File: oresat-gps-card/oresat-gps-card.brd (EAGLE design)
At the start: 99.8 x 94.7 mm, 354 parts, among them J1 ORESAT-DEBUG-CONNECTOR-CARD, J100 DM3BT-DSF-PEJS, J102 FTSH-105-XX-X-DV-K, J4 TFM-120-01-L-D-RA, Q1 MMBT2907, Q2 PMV45EN, Q3 DMP2240UDM, Q4 PMV45EN, Q5 MOSFET-PCH-SOT23-6, Q6 MOSFET-PCH-SOT23-6, U1 RCLAMP0504FB, U10 TLVH431, U11 TCAN330, U12 MIC842LYC5, U13 MIC842LYC5, U14 MAX4211FETE, U15 TPS62112, U16 MAX7310ATE, U17 25AAXX, U18 VENUS838FLPX-L, U19 BP2G+, U2 TPS2051CDBVR, U20 MAX8510EXK29+T, U21 ALM-GP003, U22 LT1719S6, U4 SN74LVC1G07DCK, U5 MAX2769ETI+, U6 7Q-16.368MBG-T, U7 OSD3358-512M-BSM, U8 MAX8510EXK29+T, U9 MAX8510EXK29+T, Y1 24MHz, Y2 ABS07-32.768KHZ-T

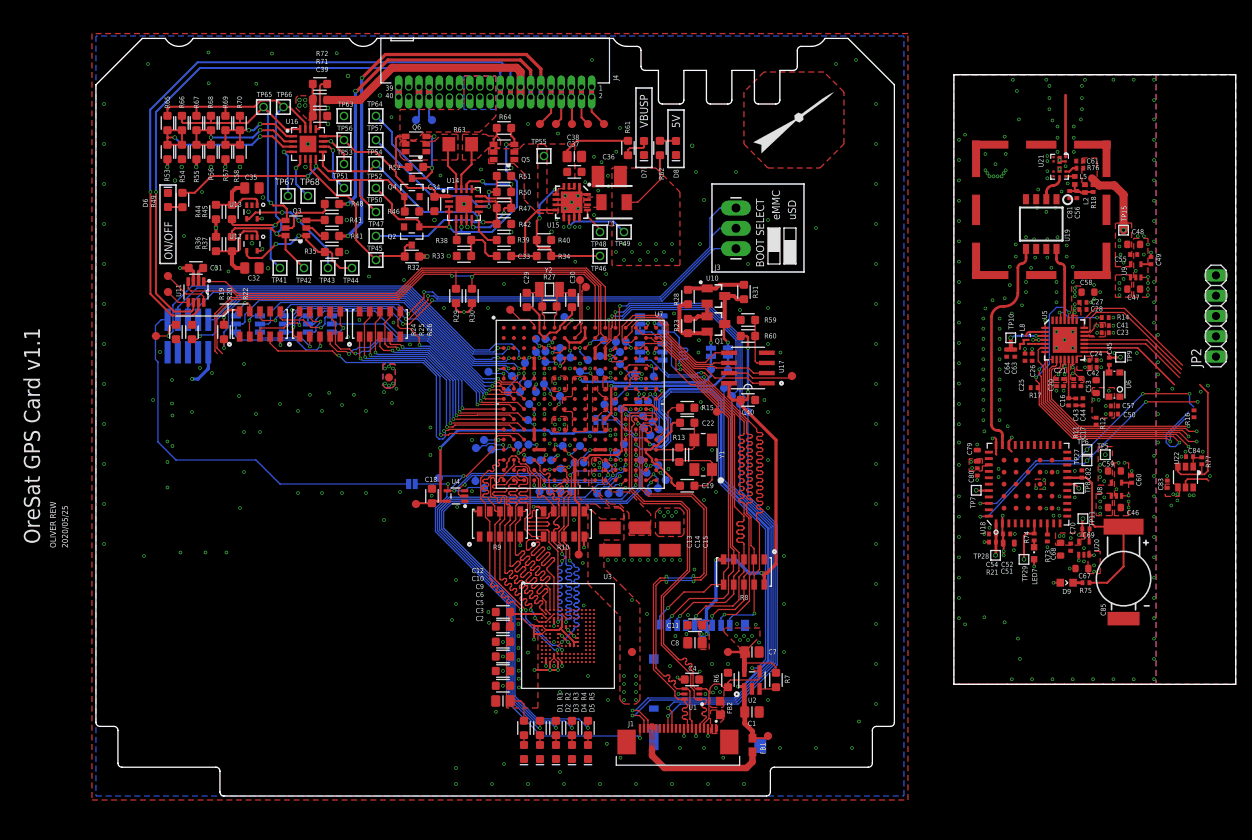
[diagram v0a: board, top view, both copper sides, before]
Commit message: GPS card has been mostly layed out. Still missing a few things, but nothing major.
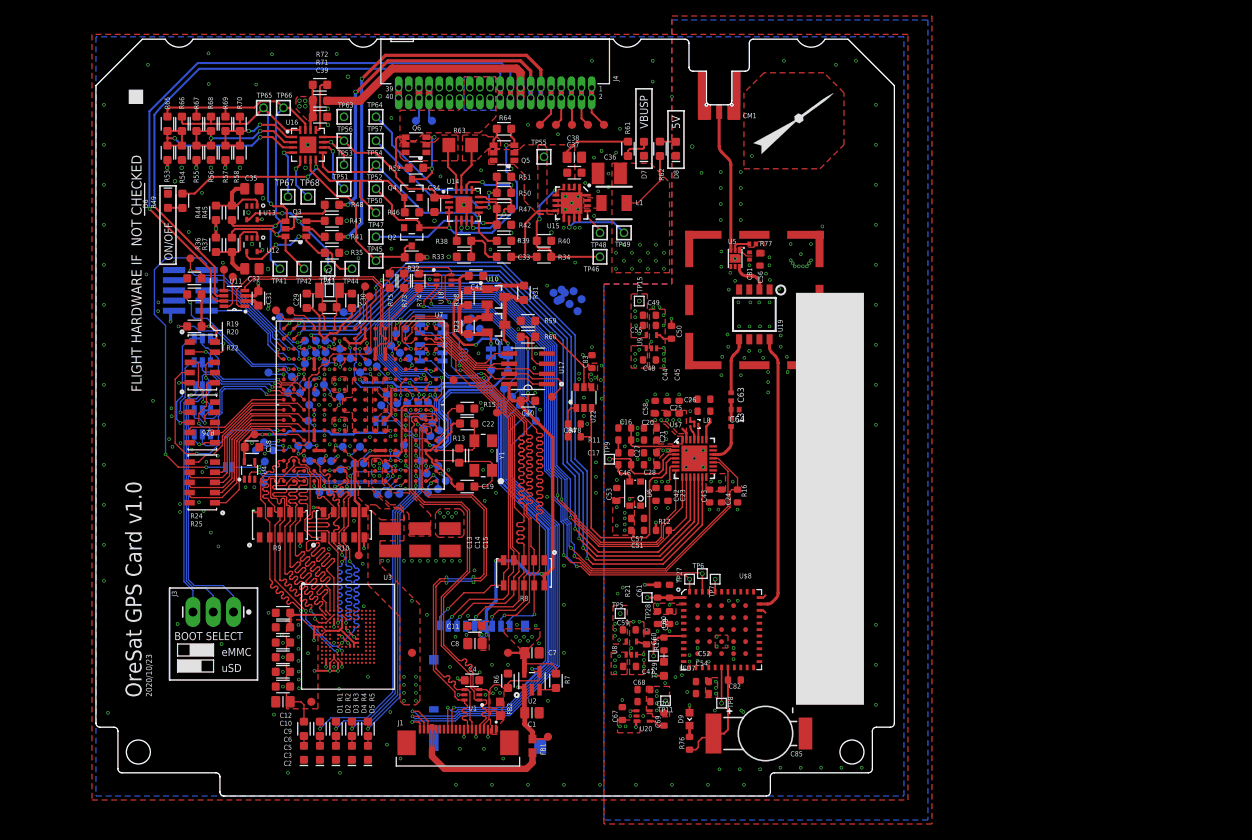
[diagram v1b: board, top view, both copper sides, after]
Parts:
- removed JP2: (no value), pinhead:1X05
- removed L2: 22n, rcl_custom:.0402-B-NOSILK
- removed L5: 1.8n, rcl_custom:.0402-B-NOSILK
- removed R14: 1k, rcl_custom:0402-C-NOSILK@1
- removed R18: 10, rcl_custom:0402-C-NOSILK@1
- removed R29, R30: 4.7k, oresat-rcl:.0603-A
- removed U21: ALM-GP003, ic-lna-ALM-GPxx-Avago:AVAGO+SAW+LNA
- added CM1: J-MOLEX-SMPM-73300-003X, J-Molex-73300-003X-SMPM-M-edge-mount:J-MOLEX-SMPM-073300-003X
- added L3: 5.6n, oresat-rcl:.0402-B-NOSILK
- added R78: 10k, oresat-rcl:.0603-B-NOSILK
- added TP12, TP13, TP16, TP17, TP18, TP19, TP20, TP21, TP23, TP24, TP26, TP32, TP33, TP34, TP36, TP37, TP70: TEST-POINT3X4, SparkFun-Connectors:PAD.03X.04
- added U$4: (no value), oresat-flight-marker:FLIGHTMARKER_OLD_BOARDS
- added U$7: MAX2771ETI+, U-Maxim-MAX2771-Multiband-Universal-GNSS-Receiver:90-0023
- added U$8: VENUS838LPX-L, U-Venus-Venus838LPxL-GPS-Module:VENUS838LPX
- C16, C17, C20, C21, C23, C24, C25, C26, C27, C28, C42, C43, C55, C56, C57, C60, C69, C70, C80, C82, C83, C84: device rcl_custom:.0402-C-NOSILK -> oresat-rcl:.0603-B-NOSILK
- C41: value 100p -> 0.1uF; device rcl_custom:.0402-C-NOSILK -> oresat-rcl:.0603-A
- C44, C54: value 100n -> 100p; device rcl_custom:.0402-C-NOSILK -> oresat-rcl:.0603-B-NOSILK
- C45: value 10n -> 100n; device rcl_custom:.0402-C-NOSILK -> oresat-rcl:.0603-B-NOSILK
- C46: value 1u -> 10n; device rcl_custom:.0603-B-NOSILK -> oresat-rcl:.0603-B-NOSILK
- C49: value 10n -> 1u; device rcl_custom:.0402-C-NOSILK -> rcl_custom:.0603-B-NOSILK
- C50: value 100n -> 10n; device rcl_custom:.0402-C-NOSILK -> oresat-rcl:.0603-B-NOSILK
- C51: value 1u -> 100n; device rcl_custom:.0603-C-NOSILK -> oresat-rcl:.0603-B-NOSILK
- C52: value 100p -> 1u; device rcl_custom:.0402-C-NOSILK -> oresat-rcl:.0603-B-NOSILK
- C53: device rcl_custom:.0603-B-NOSILK -> oresat-rcl:.0603-B-NOSILK
- C61: value 330p -> 100n; device rcl_custom:.0402-C-NOSILK -> oresat-rcl:.0603-B-NOSILK
- C63: value 100p -> 470p; device rcl_custom:.0402-C-NOSILK -> oresat-rcl:.0402-B-NOSILK
- C64: value 100n -> 1.7p; device rcl_custom:.0402-C-NOSILK -> oresat-rcl:.0402-B-NOSILK
- C79: device rcl_custom:.0603-C-NOSILK -> oresat-rcl:.0603-B-NOSILK
- C81: value 47p -> 56p
- JP107: value JUMPER-SMT_3_NO_NO_SILK -> JUMPER-SMT_3_NO_SILK; device SparkFun-Jumpers:SMT-JUMPER_3_0-NO_TRACE_NO-SILK -> SparkFun-Jumpers:SMT-JUMPER_3_NO_SILK
- LED7: value YLW -> Yellow; device led:CHIPLED_0603 -> SparkFun-LED:LED-0603
- PCB1: value ORESAT-CARD-V1.2-GENERIC-3XRF-V1.0 -> ORESAT-CARD-V1.3-GENERIC-1RF-POS2; device oresat-cards:ORESAT-CARD-V1.2-GENERIC-3XRF-V1.0 -> oresat-cards:ORESAT-CARD-V1.3-GENERIC-1RF-POS2
- R11, R12, R16, R21: device rcl_custom:0402-C-NOSILK@1 -> oresat-rcl:.0603-B-NOSILK
- R17: value 10k -> 1k; device rcl_custom:0402-C-NOSILK@1 -> oresat-rcl:.0603-B-NOSILK
- R73: value 10k -> 100; device rcl_custom:0402-C-NOSILK@1 -> oresat-rcl:.0603-A
- R74: value 1k -> 100; device rcl_custom:0402-C-NOSILK@1 -> oresat-rcl:.0603-A
- R75: device rcl_custom:0402-C-NOSILK@1 -> oresat-rcl:.0603-A
- R76: value 4.7k -> 100; device rcl_custom:0402-C-NOSILK@1 -> oresat-rcl:.0603-B-NOSILK
- TP10: value TEST-POINT15MIL-TEST-POINT -> TEST-POINT3X4; device Tova:15MIL-TEST-POINT -> SparkFun-Connectors:PAD.03X.04
- U18: value VENUS838FLPX-L -> RCLAMP0504FB; device SparkFun-RF:VENUS638FLPX -> U-Semtec-RCLAMP0504FB:SC70-6
- U5: value MAX2769ETI+ -> SKY65723-81; device max2769:90-0023 -> U-Skyworks-SKY65723-81-GPS-LNA-with-filter:SKY65723-81
- moved R75 94.9 mm to (36.7, 64.4), turned to 270 degrees
- moved R76 86.9 mm to (74.2, 6.59), turned to 90 degrees
- moved R73 86.6 mm to (38.5, 64.4), turned to 270 degrees
- moved R74 83.3 mm to (40.3, 64.4), turned to 270 degrees
- moved J3 80.6 mm to (17.2, 23.0), turned to 180 degrees
- moved C41 78.9 mm to (47.5, 65.0)
- moved C47 78.7 mm to (66.7, 16.2)
- moved U18 77.3 mm to (43.5, 64.5), turned to 270 degrees
- moved C84 77.0 mm to (59.8, 46.5), turned to 0 degrees
- moved U22 75.8 mm to (61.0, 49.8), turned to 180 degrees
- moved C61 74.3 mm to (71.7, 25.6), turned to 270 degrees
- moved C83 73.5 mm to (62.0, 54.3)
- moved TP9 65.1 mm to (64.2, 42.1)
- moved C59 63.8 mm to (66.7, 20.8)
- moved C60 63.8 mm to (68.8, 19.8)
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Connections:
- net SPARE5 renamed N$103
- removed net 3.3VD: C46.1, C47.1, C67.1, C83.1, U20.1, U20.3, U22.4, U8.1, U8.3, U9.1, U9.3
- removed net ANTBIAS: C63.1, C64.1, TP10.P$1, U5.3
- removed net D0_I: JP102.1
- removed net D1_I: JP103.1
- removed net D2_I: JP110.1
- removed net D3_I: JP111.1
- removed net LED/GPIO: R74.2, TP29.P$1, U18.7
- removed net LNA-POWER-FILTERED: C56.1, C81.1, L2.1, L5.1, R18.2
- removed net MAX_!IDLE: R17.2, U5.24
- removed net MAX_ANTFLAG: U5.1
- removed net MAX_CFG_!CS: R12.1, U5.10
- removed net MAX_CFG_SPI2_MOSI: U5.8
- removed net MAX_CFG_SPI2_SCLK: U5.9
- removed net N$103 (its old number): L5.2, U21.7
- removed net N$117 (its old number): C45.1, U6.3
- removed net N$118 (its old number): C84.1, R77.1, U22.1
- removed net N$119 (its old number): R73.2, U18.9
- removed net N$21 (its old number): U21.1
- removed net N$32 (its old number): C18.1, JP104.1, TP14.P$1, TP164.P$1, U4.5, U7.K11, U7.L11
- removed net N$50 (its old number): TP143.P$1, U7.J14
- removed net N$97: TP148.P$1, U7.G14
- removed net PGM: R14.1, U5.26
- removed net RTC: TP8.P$1, U18.17
- removed net SCL_2: R30.2, U7.A10
- removed net SDA_2: R29.2, U7.B10
- removed net STM_USART6_RX: TP27.P$1, U18.44
- removed net STM_USART6_TX: TP6.P$1, U18.42
- new net 3.3VA: C18.1, C41.1, JP104.1, TP14.P$1, TP164.P$1, U18.5, U4.5, U7.K11, U7.L11
- new net LED: R17.2, TP29.P$1, U$8.7
- new net N$114: R74.2, U7.C11, U7.D11
- new net N$115: R75.2, U7.M2
- new net N$116: R73.2, U7.C10, U7.D10
- new net N$123: C63.2, C64.2, L3.1
- new net N$124: L3.2, U$7.19
- new net N$125: LED7.C, R17.1
- new net N$126: D9.CATHODE, R76.2
- new net N$127: TP8.P$1, U$8.17
- new net N$129: TP13.P$1, U7.D16
- new net N$130: TP16.P$1, U7.D15
- new net N$131: TP17.P$1, U7.D14
- new net N$133: TP19.P$1, U7.F16
- new net N$15: TP23.P$1, U7.C4
- new net N$16: TP24.P$1, U7.C3
- new net N$17: TP26.P$1, U7.B3
- new net N$18: TP32.P$1, U7.A3
- new net RF-IN: CM1.RF, U5.3
- new net SPI1_CS0: R12.1, TP143.P$1, U$7.9, U7.J14
- new net SPI1_D0: TP36.P$1, U$7.7, U7.F14
- new net SPI1_D1: TP18.P$1, U7.E15
- new net SPI1_SCLK: TP37.P$1, U$7.8, U7.F15
- new net UART2_RX: TP147.P$1, TP27.P$1, U$8.44, U7.H16
- new net UART2_TX: TP10.P$1, TP6.P$1, U$8.42, U7.E16
- net 2.85V-S: now also C54.1, U$8.2, U$8.58; no longer C51.1, U18.2, U18.36, U18.58
- net 2.85VA: now also C45.1, C50.1, C56.1, C81.1, R77.1, U$7.2, U$7.22, U$7.27, U$7.28, U5.1; no longer C43.1, C48.1, C61.1, L2.2, R18.1, R76.1, U5.11, U5.13, U5.23, U5.4
- net 2.85VD: now also C43.1, C51.1, U$7.14, U$7.6; no longer C41.1, C50.1, U5.14, U5.19
- net 3.3V: now also C47.1, C48.1, C67.1, C83.1, U20.1, U20.3, U22.4, U8.1, U8.3, U9.1, U9.3; no longer R29.1, R30.1
- net AGND: now also C45.2, C51.2, C64.1, CM1.P$1, CM1.P$2, CM1.P$3, CM1.P$4, U$7.BODY, U$8.21, U$8.22, U$8.24, U$8.25, U$8.27, U$8.28, U$8.29, U$8.31, U$8.33, U$8.61, U$8.62, U$8.65, U$8.69, U5.GND; no longer C43.2, C50.2, C61.2, C63.2, C64.2, U18.21, U18.22, U18.24, U18.25, U18.27, U18.28, U18.29, U18.31, U18.33, U18.61, U18.62, U18.65, U18.69, U21.2, U21.3, U21.4, U21.9, U21.P$1, U21.P$2, U5.BODY
- net CPOUT: now also U$7.1; no longer U5.12
- net EEPROM_WP: now also R75.1, U18.6; no longer U7.M2
- net GND: now also C43.2, C49.2, C54.2, C61.1, U$8.10, U$8.11, U$8.15, U$8.19, U$8.4, U$8.49, U$8.5, U$8.6, U$8.60, U$8.64, U18.2; no longer C46.2, C51.2, C54.1, R14.2, R17.1, R73.1, U18.10, U18.11, U18.15, U18.19, U18.49, U18.60, U18.64
- net I0: now also TP21.P$1, U$7.12, U7.A2; no longer JP2.4, U5.20
- net I1: now also TP20.P$1, U$7.13, U7.A1; no longer JP2.5, U5.21
- net I2C0_SCL: now also R73.1, U18.3; no longer U7.C10, U7.D10
- net I2C0_SDA: now also R74.1, U18.1; no longer U7.C11, U7.D11
- net LNAOUT: now also U$7.24; no longer U5.2
- net MAX-CLKOUT: now also U7.B4; no longer JP2.1
- net MAX-RF: now also C63.1, U19.5; no longer U19.8, U5.25
- net MAX_!SHDN: now also TP148.P$1, U$7.18, U7.G14; no longer U5.7
- net MAX_CLK_OUT: now also R78.2, U$7.4; no longer R77.2, U5.16
- net MAX_LD: now also TP70.P$1, U$7.17, U7.G15; no longer U5.6
- net MIXIN: now also U$7.25; no longer U5.5
- net N$113: now also C50.2; no longer C49.2
- net N$120: now also C46.1, U6.3; no longer LED7.C, R74.1
- net N$121: now also C84.1, R78.1, U22.1; no longer D9.CATHODE, R75.2
- net N$19: now also U5.6; no longer U21.6
- net N$24: now also R77.2, U5.2; no longer R76.2, U21.8
- net N$53: now also TP12.P$1, U7.E14; no longer TP147.P$1, U7.H16
- net Q0: now also TP34.P$1, U$7.11, U7.B1; no longer JP2.3, U5.18
- net Q1: now also TP33.P$1, U$7.10, U7.B2; no longer JP2.2, U5.17
- net STQ-!RST: now also C61.2, U$8.1; no longer C54.2, U18.1
- net STQ-PPS: now also U$8.40; no longer U18.40
- net STQ-RF: now also U$8.32, U19.8; no longer U18.32, U19.5
- net STQ-VBAT: now also R76.1, U$8.18; no longer R75.1, U18.18
- net XTAL: now also C46.2, U$7.3; no longer C45.2, U5.15
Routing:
- net SPI1_CS0: track 0.00 -> 92.5 mm, vias 0 -> 2
- net UART2_RX: track 0.00 -> 84.6 mm, vias 0 -> 2
- net UART2_TX: track 0.00 -> 81.6 mm, vias 0 -> 2
- net SPI1_D0: track 0.00 -> 80.5 mm, vias 0 -> 2
- net SPI1_SCLK: track 0.00 -> 79.7 mm, vias 0 -> 2
- net I1: track 16.8 -> 94.8 mm, vias 0 -> 2
- net Q0: track 13.8 -> 90.7 mm, vias 0 -> 2
- net I0: track 17.0 -> 91.2 mm, vias 0 -> 2
- net Q1: track 13.6 -> 87.1 mm, vias 0 -> 2
- net MAX_!SHDN: track 27.2 -> 99.2 mm, vias 1 -> 3
- net MAX_LD: track 28.3 -> 96.2 mm, vias 1 -> 2
- net SDA_2: track 64.7 -> 0.00 mm
- net 3.3VA: track 0.00 -> 64.5 mm, vias 0 -> 5
- net SCL_2: track 62.3 -> 0.00 mm, vias 2 -> 0
- net N$32 (its old number): track 56.0 -> 0.00 mm, vias 3 -> 0
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- added copper zone on layer 1, net 2.85VS
- added copper zone on layer 1, net 3.3VA
- removed copper zone on layer 1, net N$32 (its old number)
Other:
- board size 99.8 x 94.7 mm -> 99.8 x 94.6 mm
- board text added: "10.5mm Solar Card Opening"
- board text added: "2020/10/23"
- board text added: "Min. Cable Length: 28.625mm FFC Cable: Molex 0151660381 29.97mm"
- board text added: "OreSat GPS Card v1.0"
- board text removed: "2020/05/25"
- board text removed: "CAMERA"
- board text removed: "OLIVER REW"
- board text removed: "OreSat GPS Card v1.1"

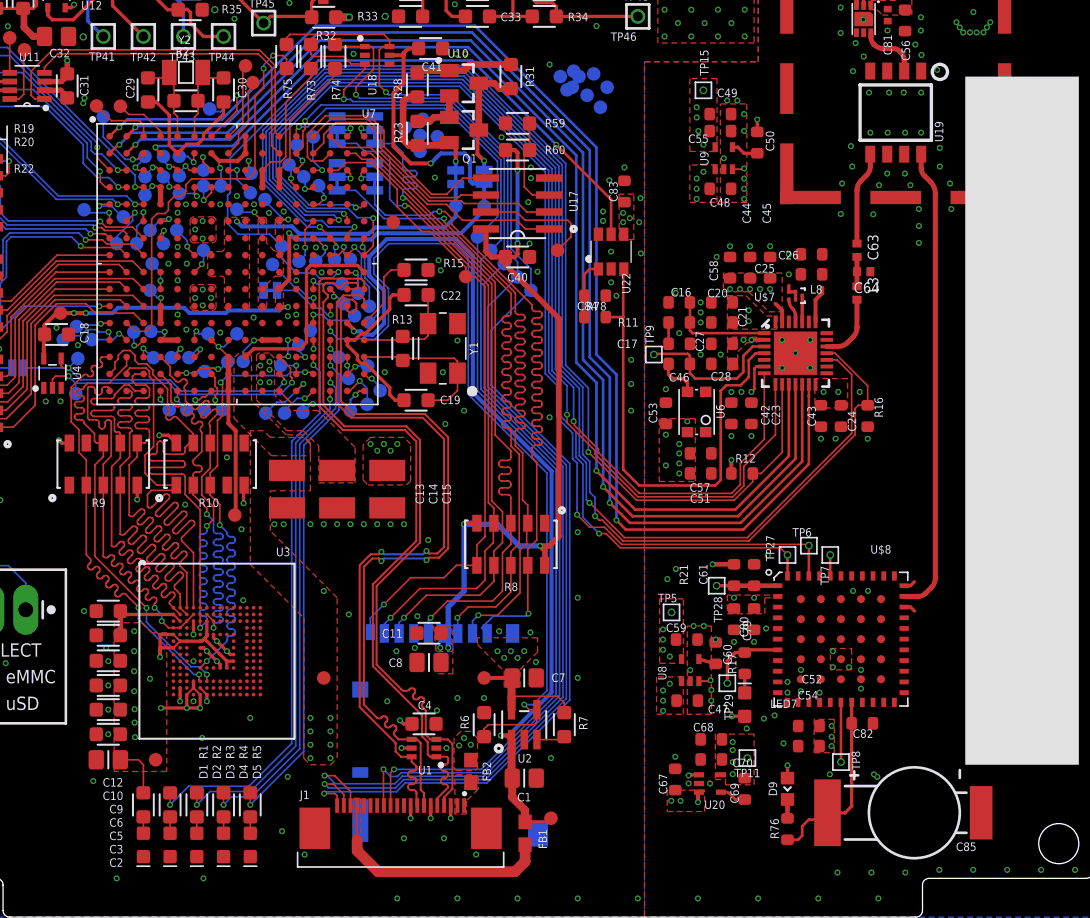
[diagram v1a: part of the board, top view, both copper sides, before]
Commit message: Added some polygons to the power plane
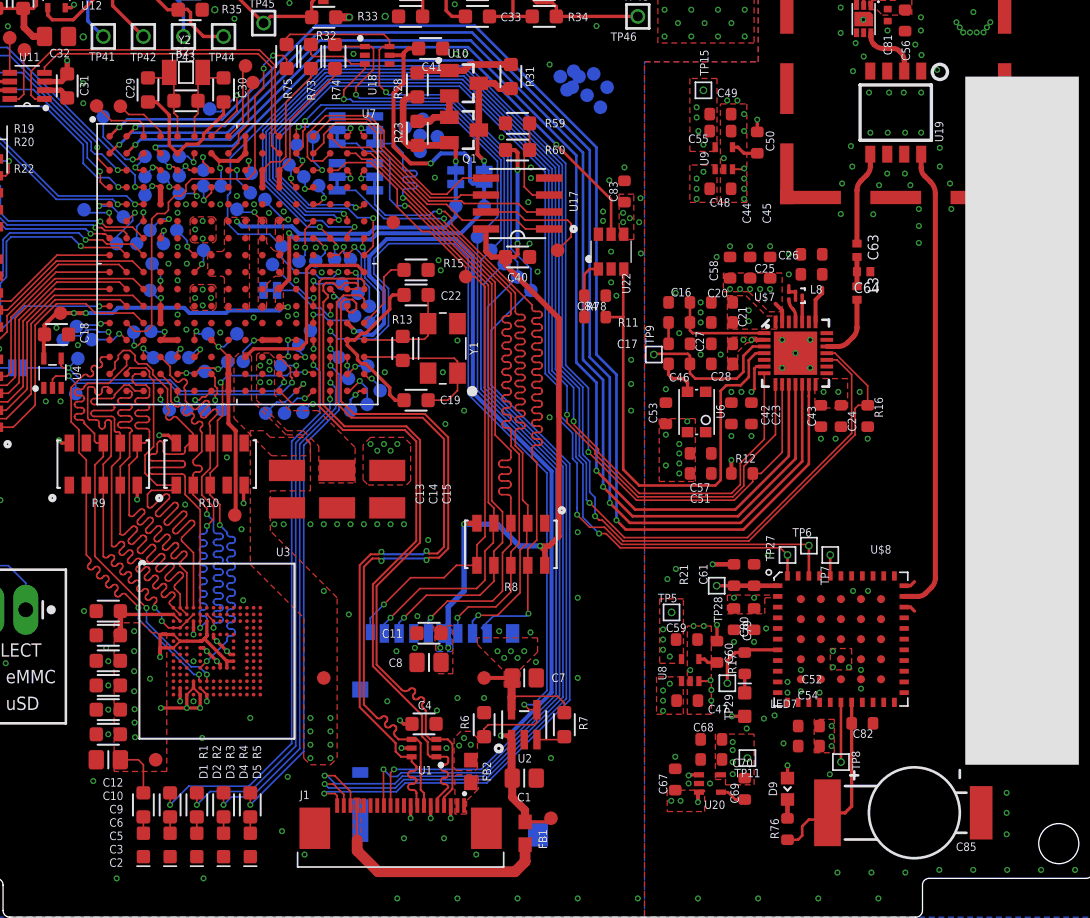
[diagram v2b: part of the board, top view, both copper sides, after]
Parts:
- moved C60 0.14 mm to (68.9, 19.9)
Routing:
- net 2.85VD: track 4.11 -> 5.11 mm
- net GND: vias 368 -> 369
- net 3.3V: vias 34 -> 45
- removed copper zone on layer 1, net 3.3VD
- removed copper zone on layer 15, net 3.3VD

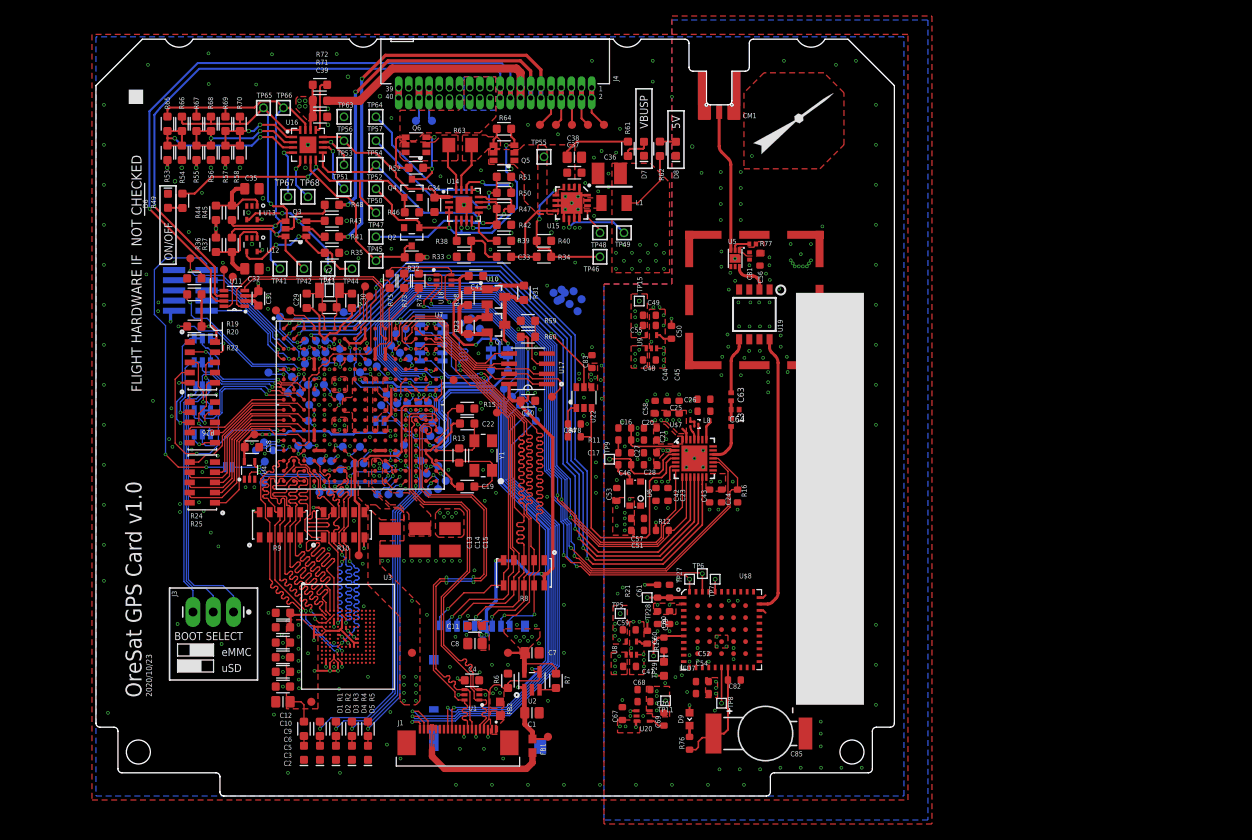
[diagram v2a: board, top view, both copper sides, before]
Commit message: Finished laying out Venus receiver. Fixed issue with GND and AGND planes. Added vias, and restrict lines to separate digital and RF ground planes. Added enable lines to Max and Venus receivers. Updated OPD circuit.
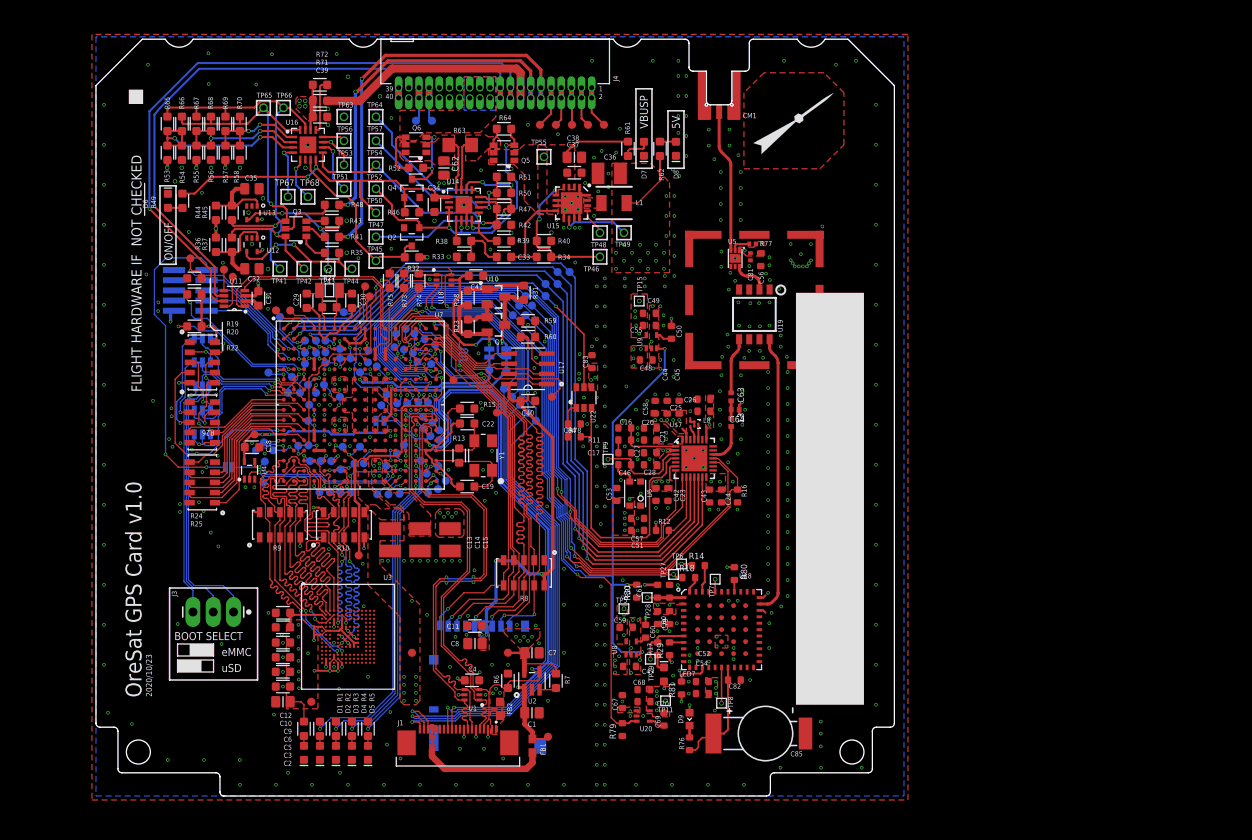
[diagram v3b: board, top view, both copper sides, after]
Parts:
- removed JP102, JP103, JP110, JP111: JUMPER-SMT_3_1-NC_TRACE_SILK, SparkFun-Jumpers:SMT-JUMPER_3_1-NC_TRACE_SILK
- added C62: 10uF, oresat-rcl:.0805-B
- added R14, R18, R29, R30, R79, R80, R81: 10k, oresat-rcl:.0603-B-NOSILK
- added TP71: TEST-POINT3X4, SparkFun-Connectors:PAD.03X.04
- R35, R43: value 10k -> 665k
- moved TP19 7.52 mm to (41.9, 54.0)
- moved TP147 7.28 mm to (53.7, 60.1)
- moved TP10 7.24 mm to (52.1, 60.1)
- moved TP18 7.16 mm to (40.2, 54.3)
- moved TP17 6.36 mm to (41.1, 57.1)
- moved TP12 5.94 mm to (39.8, 57.8)
- moved TP33 5.25 mm to (56.2, 64.0)
- moved TP70 4.92 mm to (53.7, 62.5)
- moved TP37 4.84 mm to (52.9, 61.3)
- moved TP16 4.79 mm to (42.4, 56.4)
- moved TP36 3.14 mm to (54.5, 61.3)
- moved TP6 2.86 mm to (73.2, 29.0)
- moved TP20 2.45 mm to (59.2, 65.5)
- moved TP21 2.26 mm to (57.7, 65.5)
- moved TP27 2.09 mm to (72.2, 27.7)
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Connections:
- removed net AGND: C16.2, C17.2, C20.2, C21.2, C25.2, C26.2, C27.2, C28.2, C44.2, C45.2, C51.2, C53.2, C56.2, C57.2, C58.2, C64.1, C81.2, CM1.P$1, CM1.P$2, CM1.P$3, CM1.P$4, L8.2, L8.3, L8.5, SH1.P$1, SH1.P$10, SH1.P$11, SH1.P$12, SH1.P$2, SH1.P$3, SH1.P$4, SH1.P$5, SH1.P$6, SH1.P$7, SH1.P$8, SH1.P$9, U$7.BODY, U$8.21, U$8.22, U$8.24, U$8.25, U$8.27, U$8.28, U$8.29, U$8.31, U$8.33, U$8.61, U$8.62, U$8.65, U$8.69, U19.1, U19.3, U19.4, U19.6, U19.7, U5.GND, U6.1, U6.2
- removed net MAX4211-3V3: C34.1, TP56.1, U14.1, U16.12
- removed net N$132: JP102.2, U7.C15
- removed net N$133: TP19.P$1, U7.F16
- removed net N$50: JP103.2, U7.C16
- removed net SPI1_D1: TP18.P$1, U7.E15
- new net MAX-EN: R30.2, TP19.P$1, U7.F16, U8.3, U9.3
- new net N$122: R18.2, U$8.44
- new net N$134: R29.2, U$8.8
- new net N$137: Q3.3, R43.2
- new net N$138: Q3.1, R35.2
- new net N$139: TP56.1, U16.12
- new net N$97: R14.2, U$8.42
- new net STQ-EN: R79.2, TP18.P$1, U20.3, U7.E15
- net 2.85V-S: now also R29.1, R80.1, R81.1
- net 3.3V: no longer U20.3, U8.3, U9.3
- net GND: now also C16.2, C17.2, C20.2, C21.2, C25.2, C26.2, C27.2, C28.2, C44.2, C45.2, C51.2, C53.2, C56.2, C57.2, C58.2, C62.2, C64.1, C81.2, CM1.P$1, CM1.P$2, CM1.P$3, CM1.P$4, L8.2, L8.3, L8.5, R30.1, R79.1, SH1.P$1, SH1.P$10, SH1.P$11, SH1.P$12, SH1.P$2, SH1.P$3, SH1.P$4, SH1.P$5, SH1.P$6, SH1.P$7, SH1.P$8, SH1.P$9, U$7.BODY, U$8.21, U$8.22, U$8.24, U$8.25, U$8.27, U$8.28, U$8.29, U$8.31, U$8.33, U$8.61, U$8.62, U$8.65, U$8.69, U19.1, U19.3, U19.4, U19.6, U19.7, U5.GND, U6.1, U6.2; no longer R35.1, R43.1
- net MAX-CLKOUT: now also TP71.P$1
- net N$21: now also R80.2, U$8.37; no longer JP111.2, U7.A16
- net N$27: now also R35.1; no longer Q3.1, R35.2
- net N$32: now also R81.2, U$8.14; no longer JP110.2, U7.A15
- net N$4: now also U7.C16; no longer JP103.3
- net N$5: now also U7.C15; no longer JP102.3
- net N$580: now also R43.1; no longer Q3.3, R43.2
- net N$8: now also U7.A16; no longer JP111.3
- net N$9: now also U7.A15; no longer JP110.3
- net N$98: now also C62.1
- net ON/!OFF: now also C34.1, U14.1
- net UART2_RX: now also R18.1; no longer U$8.44
- net UART2_TX: now also R14.1; no longer U$8.42
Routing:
- net MAX-EN: track 0.00 -> 117.9 mm, vias 0 -> 4
- net STQ-EN: track 0.00 -> 86.2 mm, vias 0 -> 2
- net MAX4211-3V3: track 19.6 -> 0.00 mm
- net ON/!OFF: track 38.5 -> 45.6 mm
- net N$53: track 0.00 -> 7.08 mm, vias 0 -> 1
- net GND: track 30.6 -> 36.1 mm, vias 369 -> 502
- net 3.3V: track 103.5 -> 98.7 mm, vias 45 -> 40
- net 2.85V-S: track 3.81 -> 7.97 mm, vias 15 -> 18
- net I1: track 94.8 -> 99.0 mm
- net N$131: track 0.00 -> 3.74 mm, vias 0 -> 1
- net N$138: track 0.00 -> 3.71 mm
- net I0: track 91.2 -> 94.9 mm
- net N$129: track 0.00 -> 3.52 mm
- net N$97: track 0.00 -> 3.39 mm
- net AGND: track 3.34 -> 0.00 mm, vias 8 -> 0
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- added copper zone on layer 15, net N$132
- added copper zone on layer 2, net N$135
- added copper zone on layer 2, net N$136
- added copper zone on layer 15, net N$50
- removed copper zone on layer 1, net 2.85VS
- removed copper zone on layer 1, net AGND
- removed copper zone on layer 15, net AGND
- removed copper zone on layer 16, net AGND
- removed copper zone on layer 2, net AGND
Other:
- board text removed: "10.5mm Solar Card Opening"
